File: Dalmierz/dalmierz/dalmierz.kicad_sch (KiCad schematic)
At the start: 7 parts, among them J1 690-005-298-486, U1 RP2040, U2 RT6150B-33GQW

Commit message: MAIN: work in progress.
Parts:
- added C15: 100n, symbol Device:C
- added C18: 2u2, symbol Device:C
- added C2: 47u, symbol Device:C
- added C3: 1n, symbol Device:C
- added D2: Green, symbol Device:LED
- added IC1: W25Q16JVUXIQ, W25Q16JVUXIQ:SON50P300X200X60-9N, symbol W25Q16JVUXIQ:W25Q16JVUXIQ
- added J2: ~, symbol CON_PICO_40W:CON_PICO_40W
- added Q1: DMG1012T, Package_TO_SOT_SMD:SOT-523, symbol Transistor_FET:DMG1012T
- added R1: 10k, symbol Device:R
- added R10: 5k6, symbol Device:R
- added R3: 470R, symbol Device:R
- added R5: 200k, symbol Device:R
- added R6: 100k, symbol Device:R
- added SW1: ~, symbol TP-1221U-K9K5325:TP-1221U-K9K5325
- added Y1: ABLS2-12.000MHZ-D4Y-T, ABLS2-12.000MHZ-D4Y-T:XTAL_ABLS2-12.000MHZ-D4Y-T, symbol ABLS2-12.000MHZ-D4Y-T:ABLS2-12.000MHZ-D4Y-T
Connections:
- net GND: now also C15.2, C18.2, C2.2, C3.2, D2.1 (K), IC1.4 (GND), J2.13, J2.18, J2.23, J2.28, J2.3, J2.38, J2.8, R1.2, R6.2, SW1.3, SW1.4
- net GPIO0: now also J2.1
- net GPIO1: now also J2.2
- net GPIO10: now also J2.14
- net GPIO11: now also J2.15
- net GPIO12: now also J2.16
- net GPIO13: now also J2.17
- net GPIO14: now also J2.19
- net GPIO15: now also J2.20
- net GPIO16: now also J2.21
- net GPIO17: now also J2.22
- net GPIO18: now also J2.24
- net GPIO19: now also J2.25
- net GPIO2: now also J2.4
- net GPIO20: now also J2.26
- net GPIO21: now also J2.27
- net GPIO22: now also J2.29
- net GPIO24: now also R1.1, R10.2
- net GPIO25: now also R3.1
- net GPIO26_ADC0: now also J2.31
- net GPIO27_ADC1: now also J2.32
- net GPIO28_ADC2: now also J2.34
- net GPIO29_ADC3: now also Q1.2 (S)
- net GPIO3: now also J2.5
- net GPIO4: now also J2.6
- net GPIO5: now also J2.7
- net GPIO6: now also J2.9
- net GPIO7: now also J2.10
- net GPIO8: now also J2.11
- net GPIO9: now also J2.12
- net QSPI_SD0: now also IC1.5 (DI_(IO0))
- net QSPI_SD1: now also IC1.2 (DO_(IO1))
- net RUN: now also J2.30
- net +3V3: now reaches U2.1 (VOUT)
- net +3V3: now also C15.1, C18.1, C2.1, IC1.8 (VCC), J2.36, Q1.1 (G)
- net at D1.1, U2.5 (VIN): now also U2.8 (VINA)
- net VBUS: now reaches D1.2, J1.1 (VBUS)
- net VBUS: now also J2.40, R10.1
- new net: SW1.1, SW1.2
- new net: D2.2 (A), R3.2
- new net: C3.1, Q1.3 (D), R5.2, R6.1
- new net 3V3_EN: J2.37
- new net ADC_VREF: J2.35
- no-connect marks 0 -> 1
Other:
- moved on the sheet: J1, L1

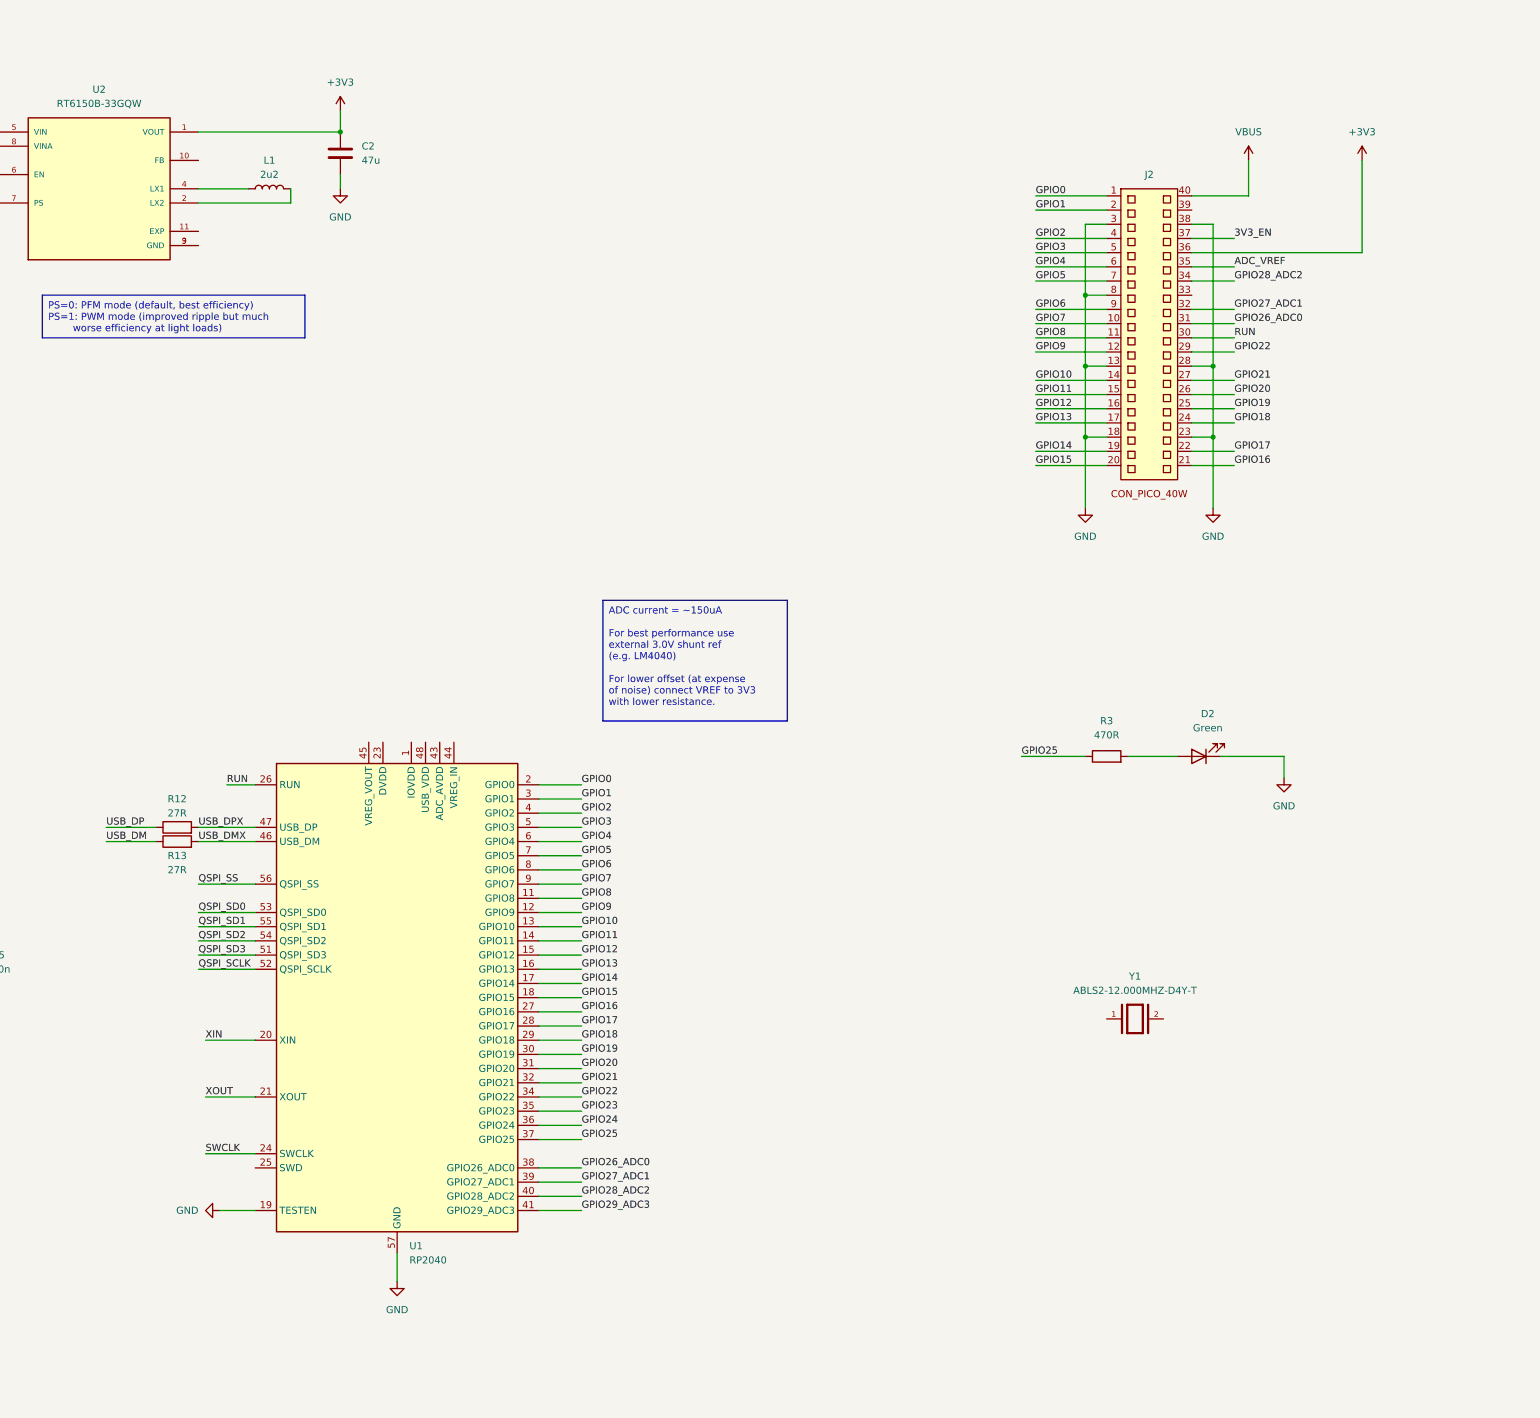
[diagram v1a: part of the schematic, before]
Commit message: MAIN: Resolved issues: missing IOVDD, DVDD pins. Updated RP2040.
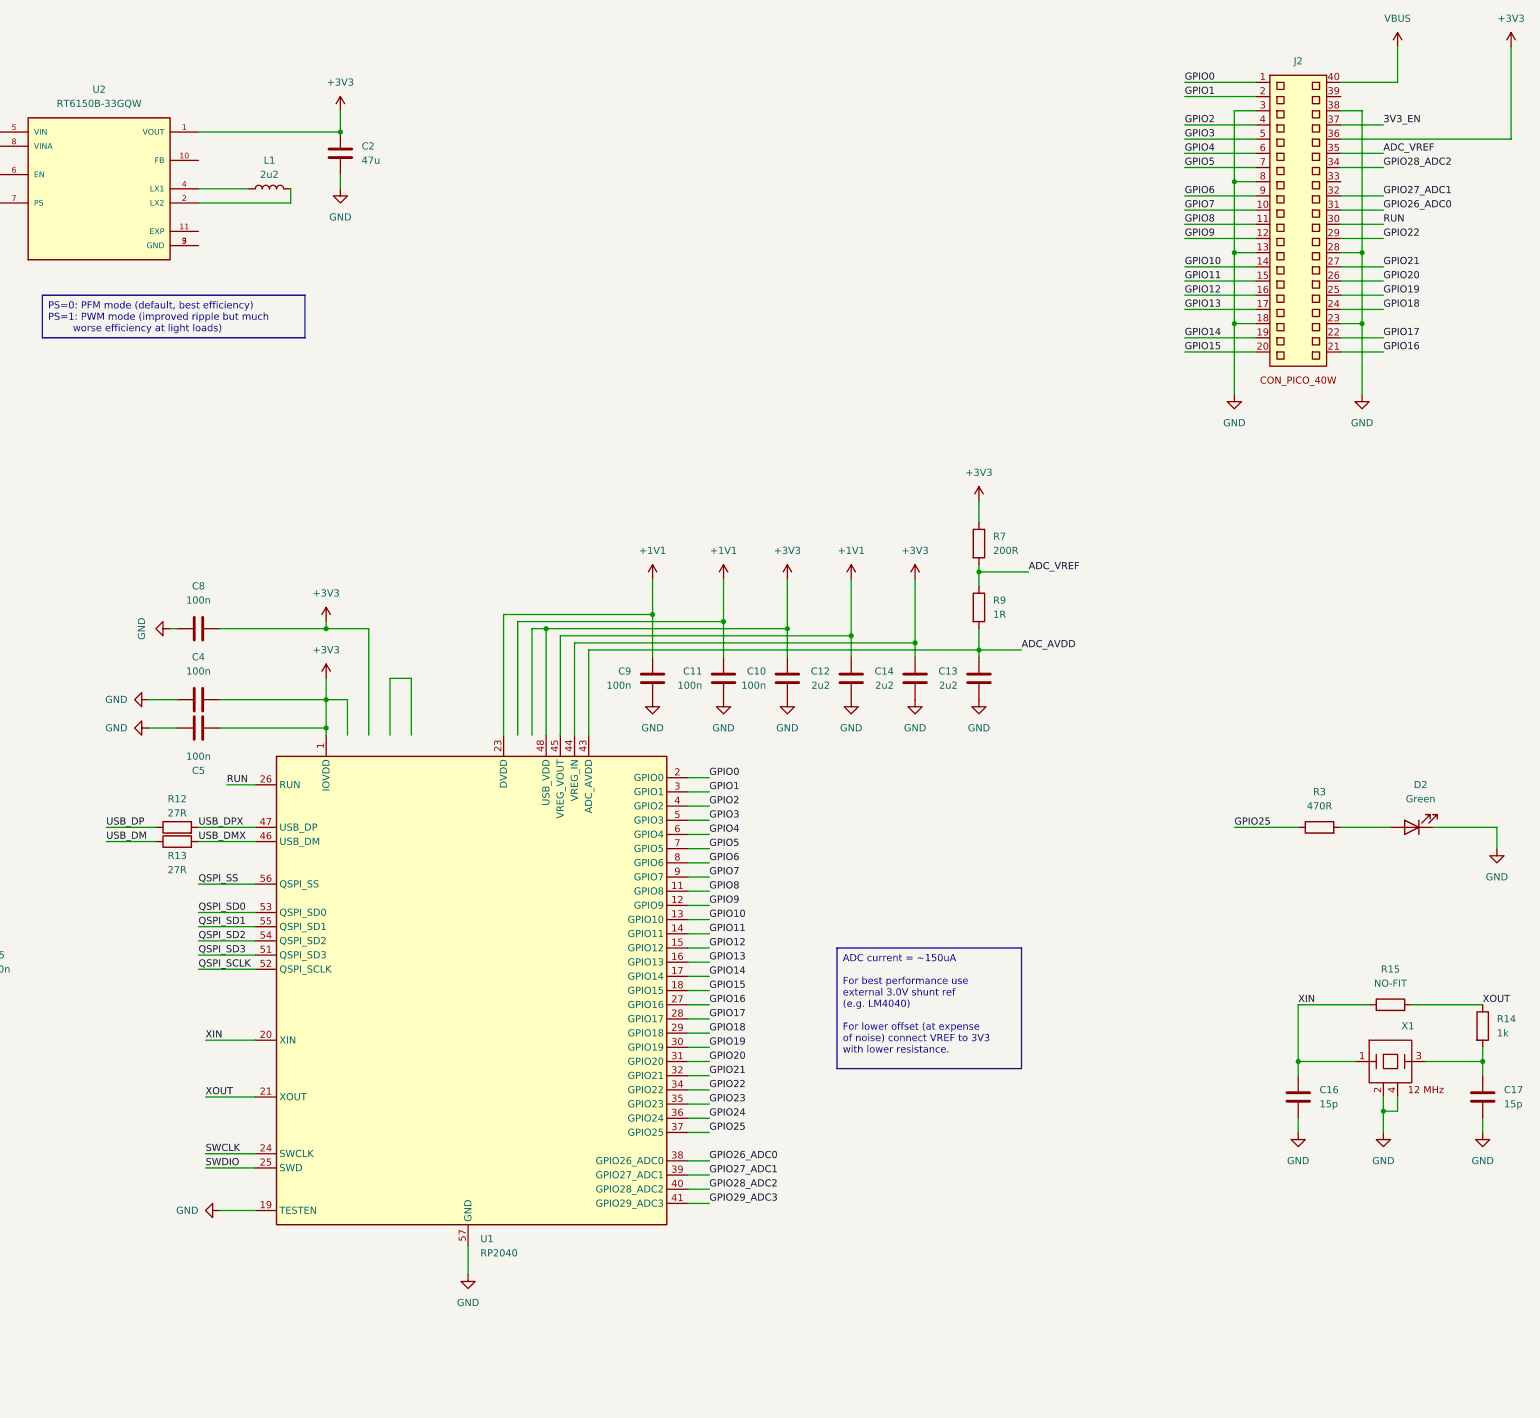
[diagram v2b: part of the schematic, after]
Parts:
- removed U1: RP2040, Package_DFN_QFN:QFN-56-1EP_7x7mm_P0.4mm_EP3.2x3.2mm, symbol MCU_RaspberryPi:RP2040
- removed Y1: ABLS2-12.000MHZ-D4Y-T, ABLS2-12.000MHZ-D4Y-T:XTAL_ABLS2-12.000MHZ-D4Y-T, symbol ABLS2-12.000MHZ-D4Y-T:ABLS2-12.000MHZ-D4Y-T
- added C10, C11, C4, C5, C8, C9: 100n, symbol Device:C
- added C12, C13, C14: 2u2, symbol Device:C
- added C16, C17: 15p, symbol Device:C
- added R14: 1k, symbol Device:R
- added R15: NO-FIT, symbol Device:R
- added R7: 200R, symbol Device:R
- added R9: 1R, symbol Device:R
- added U1: RP2040, Package_DFN_QFN:QFN-56-1EP_7x7mm_P0.4mm_EP3.2x3.2mm, symbol RP2040_CUSTOM:RP2040
- added X1: ~, symbol X1_12MHZ:12MHz
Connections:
- net +3V3: now also C10.1, C14.1, C4.2, C5.2, C8.2, R7.1, U1.1 (IOVDD), U1.10 (IOVDD), U1.22 (IOVDD), U1.44 (VREG_IN), U1.48 (USB_VDD), U1.49 (IOVDD)
- net ADC_VREF: now also R7.2, R9.1
- net GND: now also C10.2, C11.2, C12.2, C13.2, C14.2, C16.2, C17.2, C4.1, C5.1, C8.1, C9.2, U1.19 (TESTEN), U1.57 (GND), X1.2, X1.4
- net GPIO0: now also U1.2 (GPIO0)
- net GPIO1: now also U1.3 (GPIO1)
- net GPIO10: now also U1.13 (GPIO10)
- net GPIO11: now also U1.14 (GPIO11)
- net GPIO12: now also U1.15 (GPIO12)
- net GPIO13: now also U1.16 (GPIO13)
- net GPIO14: now also U1.17 (GPIO14)
- net GPIO15: now also U1.18 (GPIO15)
- net GPIO16: now also U1.27 (GPIO16)
- net GPIO17: now also U1.28 (GPIO17)
- net GPIO18: now also U1.29 (GPIO18)
- net GPIO19: now also U1.30 (GPIO19)
- net GPIO2: now also U1.4 (GPIO2)
- net GPIO20: now also U1.31 (GPIO20)
- net GPIO21: now also U1.32 (GPIO21)
- net GPIO22: now also U1.34 (GPIO22)
- net GPIO23: now also U1.35 (GPIO23)
- net GPIO24: now also U1.36 (GPIO24)
- net GPIO25: now also U1.37 (GPIO25)
- net GPIO26_ADC0: now also U1.38 (GPIO26_ADC0)
- net GPIO27_ADC1: now also U1.39 (GPIO27_ADC1)
- net GPIO28_ADC2: now also U1.40 (GPIO28_ADC2)
- net GPIO29_ADC3: now also U1.41 (GPIO29_ADC3)
- net GPIO3: now also U1.5 (GPIO3)
- net GPIO4: now also U1.6 (GPIO4)
- net GPIO5: now also U1.7 (GPIO5)
- net GPIO6: now also U1.8 (GPIO6)
- net GPIO7: now also U1.9 (GPIO7)
- net GPIO8: now also U1.11 (GPIO8)
- net GPIO9: now also U1.12 (GPIO9)
- net QSPI_SCLK: now also U1.52 (QSPI_SCLK)
- net QSPI_SD0: now also U1.53 (QSPI_SD0)
- net QSPI_SD1: now also U1.55 (QSPI_SD1)
- net QSPI_SD2: now also U1.54 (QSPI_SD2)
- net QSPI_SD3: now also U1.51 (QSPI_SD3)
- net QSPI_SS: now also U1.56 (QSPI_SS)
- net RUN: now also U1.26 (RUN)
- net SWCLK: now also U1.24 (SWCLK)
- net USB_DMX: now also U1.46 (USB_DM)
- net USB_DPX: now also U1.47 (USB_DP)
- net XIN: now also C16.1, R15.1, U1.20 (XIN), X1.1
- net XOUT: now also R14.1, R15.2, U1.21 (XOUT)
- new net: C17.1, R14.2, X1.3
- new net: U1.33 (IOVDD), U1.42 (IOVDD)
- new net +1V1: C11.1, C12.1, C9.1, U1.23 (DVDD), U1.45 (VREG_VOUT), U1.50 (DVDD)
- new net ADC_AVDD: C13.1, R9.2, U1.43 (ADC_AVDD)
- new net SWDIO: U1.25 (SWD)
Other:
- moved on the sheet: D2, J2, R3

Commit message: Main: dodalem odpowiedzi na pytania.
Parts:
- added C6, C7: 100n, symbol Device:C
- added J3: ~, symbol CON_PICO_3W:CON_PICO_3W
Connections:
- net +3V3: now also U1.33 (IOVDD), U1.42 (IOVDD), C6.2, C7.2
- net GND: now also C6.1, C7.1, J3.2
- net SWCLK: now also J3.1
- net SWDIO: now also J3.3
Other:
- moved on the sheet: C8

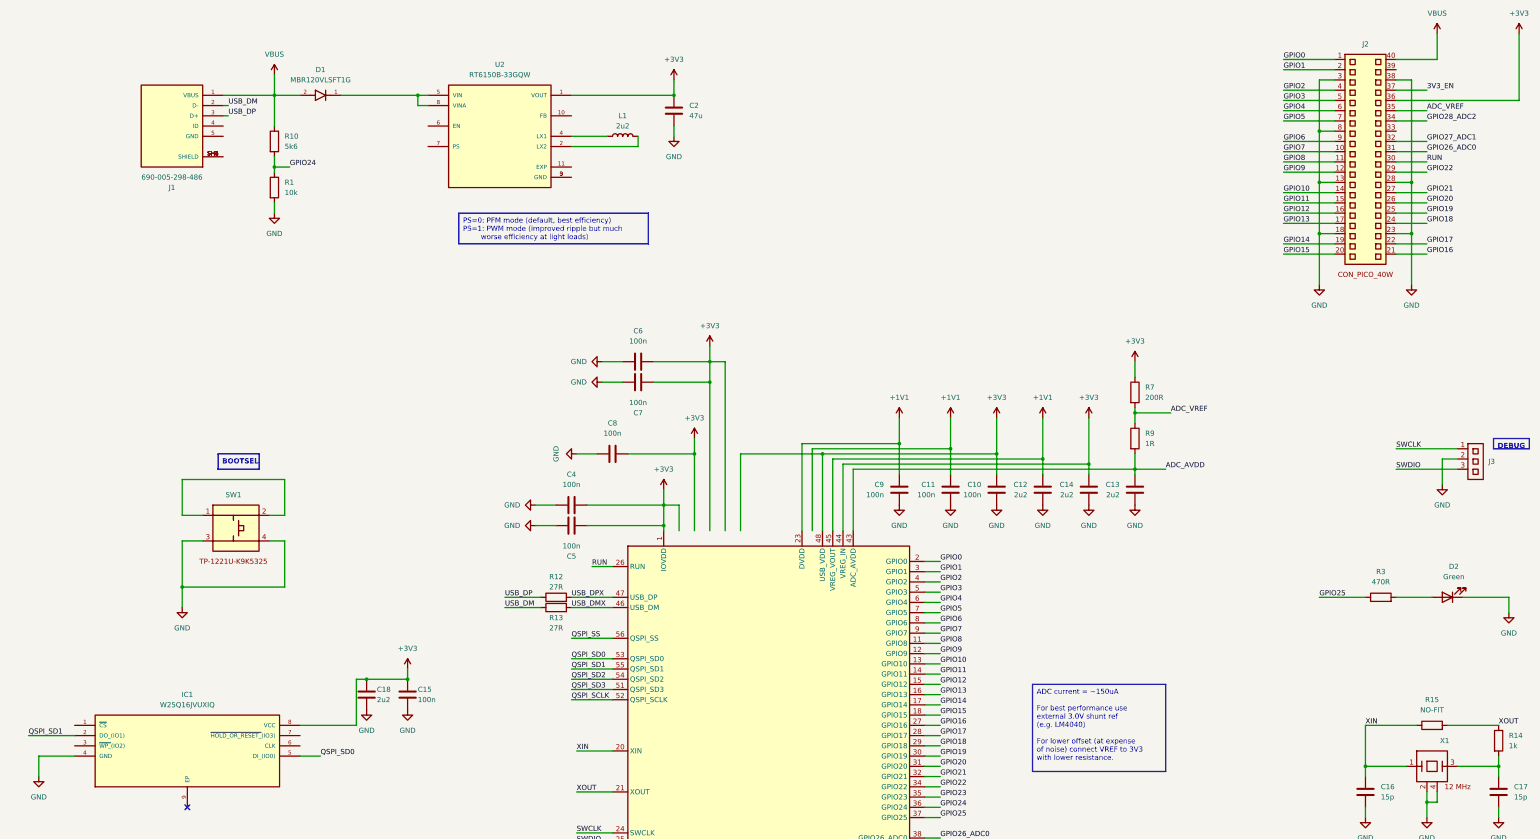
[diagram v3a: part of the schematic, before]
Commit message: MAIN: dalmierz work in progress.
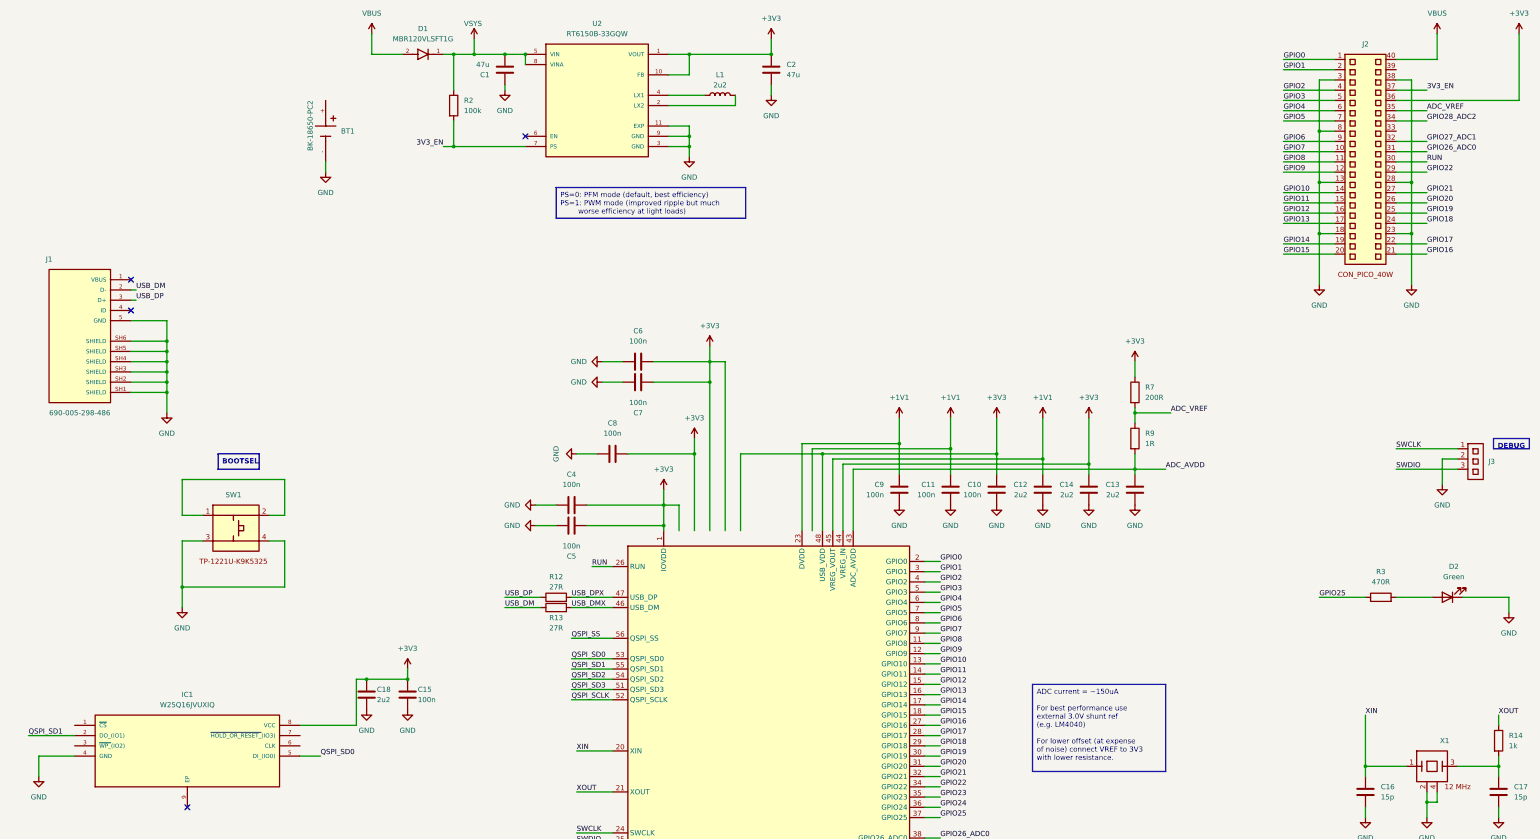
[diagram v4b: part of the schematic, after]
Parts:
- removed R1: 10k, symbol Device:R
- removed R10: 5k6, symbol Device:R
- removed R15: NO-FIT, symbol Device:R
- added BT1: BK-18650-PC2, BK-18650-PC2:BAT_BK-18650-PC2, symbol BK-18650-PC2:BK-18650-PC2
- added C1: 47u, symbol Device:C
- added R2: 100k, symbol Device:R
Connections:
- net +3V3: now also U2.10 (FB)
- net 3V3_EN: now also U2.7 (PS), R2.2
- net GND: now also J1.5 (GND), J1.SH1 (SHIELD), J1.SH2 (SHIELD), J1.SH3 (SHIELD), J1.SH4 (SHIELD), J1.SH5 (SHIELD), J1.SH6 (SHIELD), U2.11 (EXP), U2.3 (GND), U2.9 (GND), BT1.-, C1.1
- net VBUS: no longer J1.1 (VBUS)
- net at D1.1, U2.5 (VIN), U2.8 (VINA): now also C1.2, R2.1
- no-connect marks 1 -> 4
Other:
- moved on the sheet: C2, D1, L1

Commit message: MAIN: dalmierz.sch work in progress.
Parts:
- added C19: 1u, symbol Device:C
- added U3: LC709203FQH-01TWG, Package_DFN_QFN:WDFN-8-1EP_4x3mm_P0.65mm_EP2.4x1.8mm, symbol Battery_Management:LC709203FQH-01TWG
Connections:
- net GND: now also C19.1, U3.1 (TEST), U3.2 (V_{SS}), U3.4 (~{ALARMB})
- net VBUS: now also BT1.+, C19.2, U3.3 (V_{DD})
- net GPIO0 renamed SDA0
- net SDA0: now also U3.7 (SDA)
- net GPIO1 renamed SCL0
- net SCL0: now also U3.8 (SCL)
- no-connect marks 4 -> 7
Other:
- moved on the sheet: BT1, C1, C2, D1, R2, U2
